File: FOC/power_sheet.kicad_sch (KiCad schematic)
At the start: 2 parts, among them U4 AP2112K-3.3

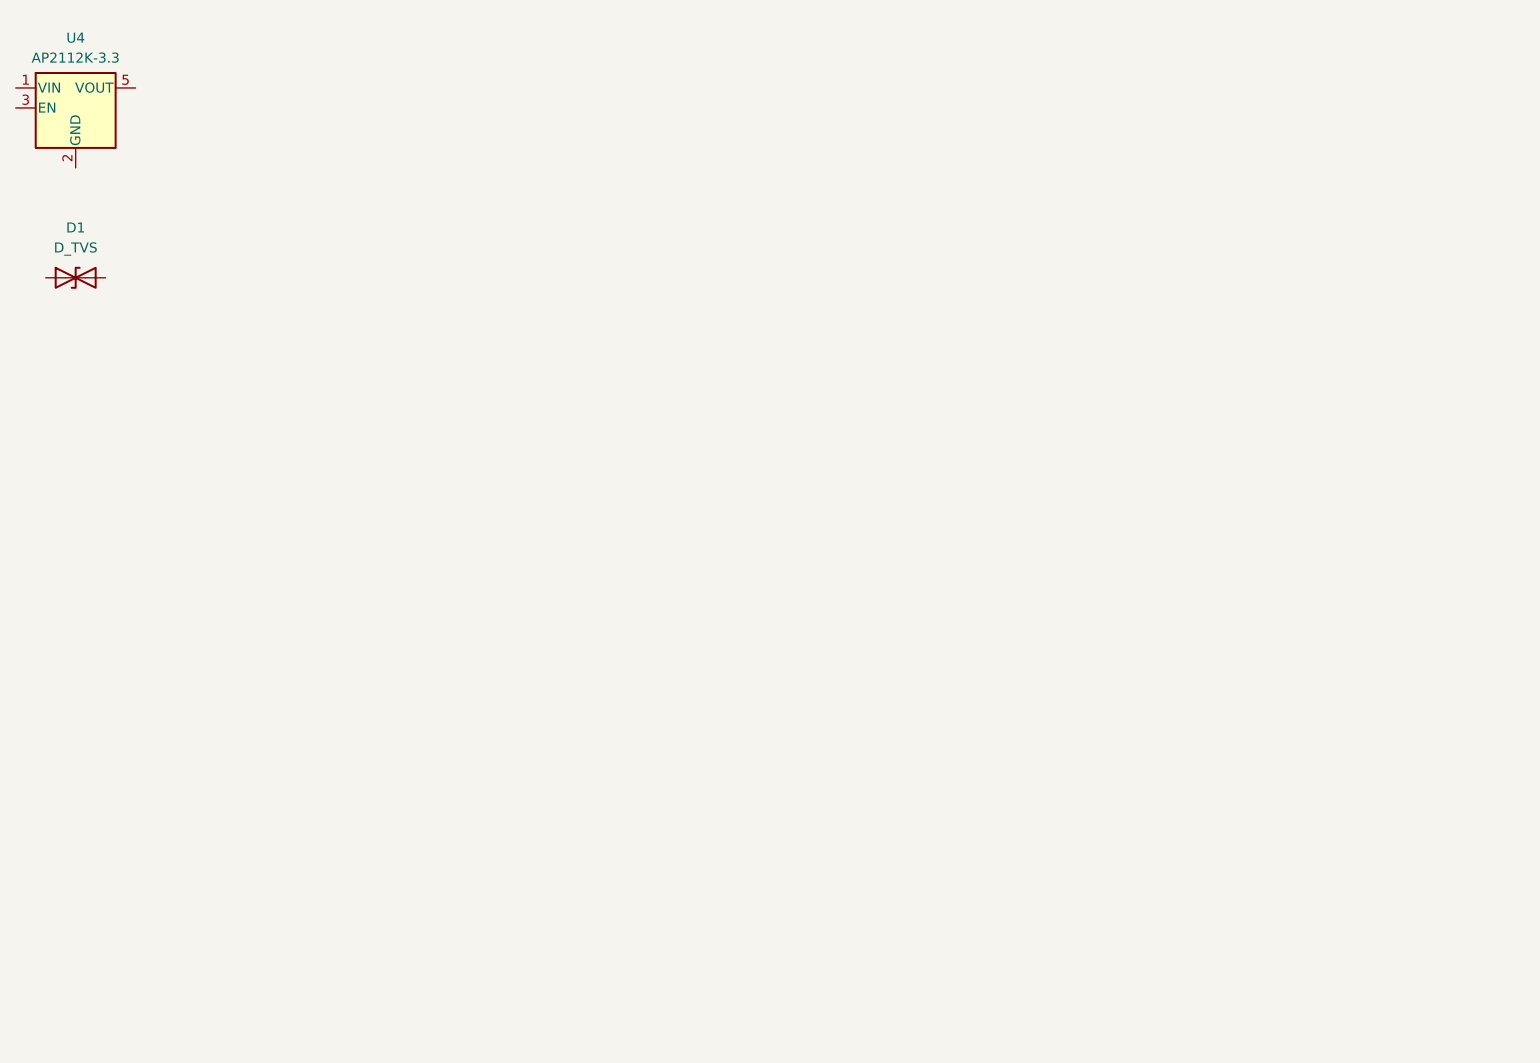
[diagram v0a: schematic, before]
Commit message: CAN + UART done;driver controller done
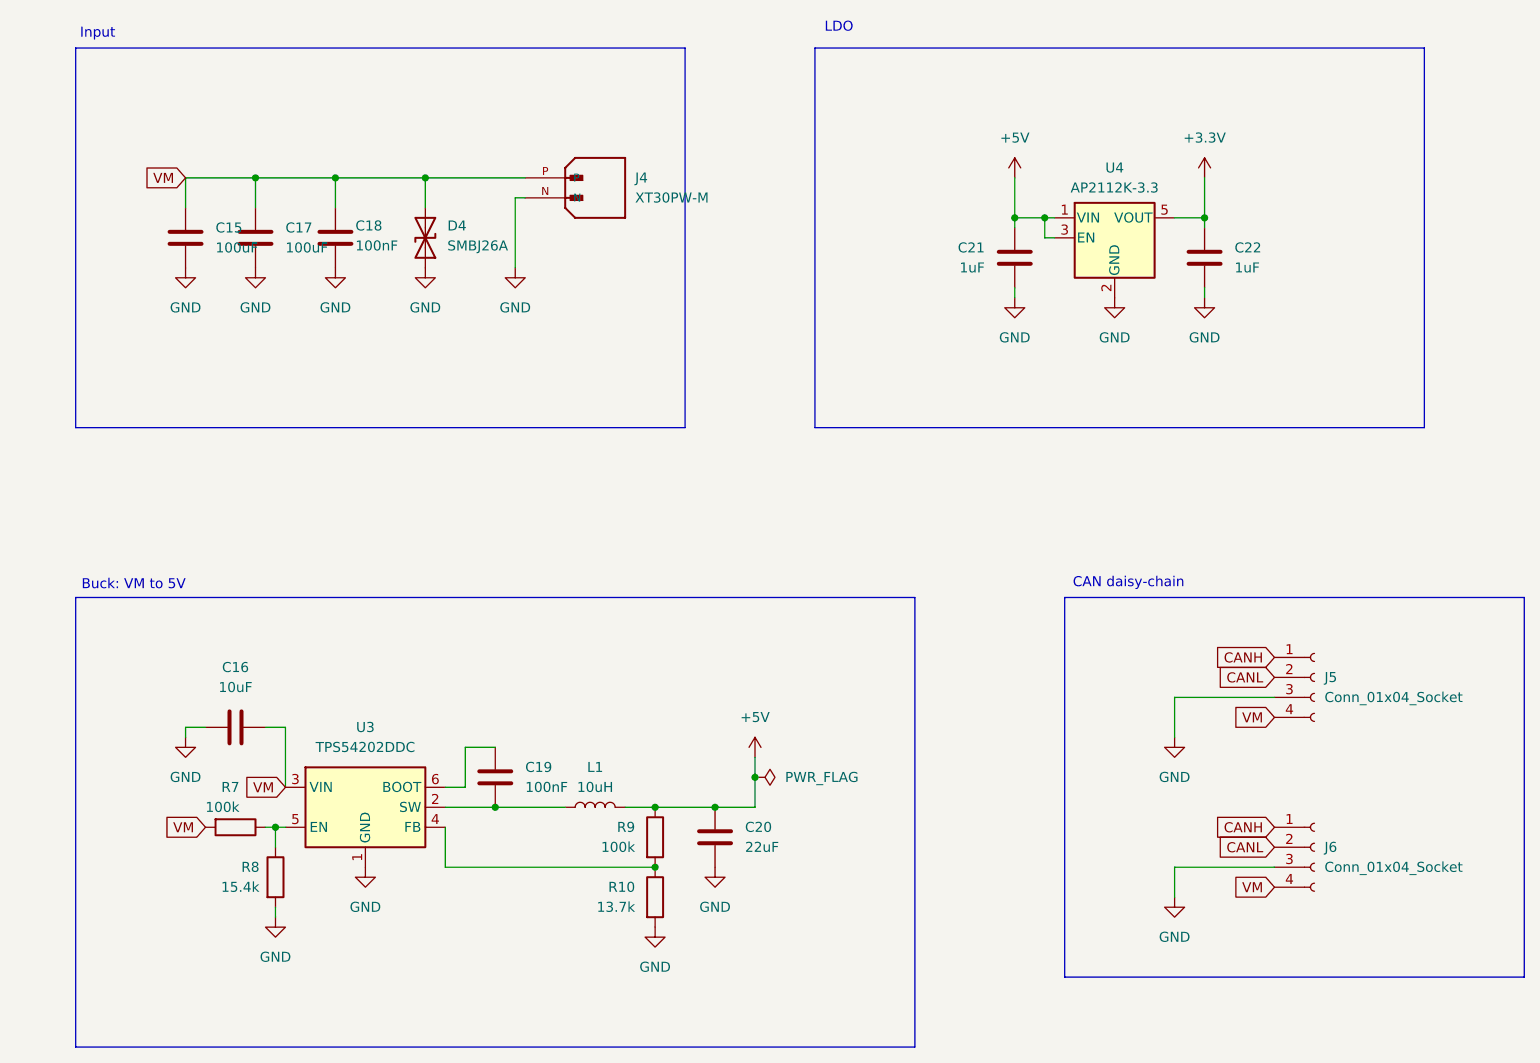
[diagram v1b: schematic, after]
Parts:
- added C15, C17: 100uF, Capacitor_SMD:CP_Elec_6.3x7.7, symbol Device:C
- added C16: 10uF, Capacitor_SMD:C_0603_1608Metric, symbol Device:C
- added C18, C19: 100nF, Capacitor_SMD:C_0603_1608Metric, symbol Device:C
- added C20: 22uF, Capacitor_SMD:C_0805_2012Metric, symbol Device:C
- added C21, C22: 1uF, Capacitor_SMD:C_0603_1608Metric, symbol Device:C
- added J4: XT30PW-M, XT30PW-M:AMASS_XT30PW-M, symbol XT30PW-M:XT30PW-M
- added J5, J6: Conn_01x04_Socket, Connector_JST:JST_GH_SM04B-GHS-TB_1x04-1MP_P1.25mm_Horizontal, symbol Connector:Conn_01x04_Socket
- added L1: 10uH, Inductor_SMD:L_Taiyo-Yuden_NR-40xx, symbol Device:L
- added R10: 13.7k, Resistor_SMD:R_0603_1608Metric, symbol Device:R
- added R7, R9: 100k, Resistor_SMD:R_0603_1608Metric, symbol Device:R
- added R8: 15.4k, Resistor_SMD:R_0603_1608Metric, symbol Device:R
- added U3: TPS54202DDC, Package_TO_SOT_SMD:SOT-23-6, symbol Regulator_Switching:TPS54202DDC
- D4: renamed from D1; value D_TVS -> SMBJ26A; footprint (none) -> Diode_SMD:D_SMB
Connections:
- net +5V: now reaches U4.1 (VIN)
- net +5V: now also U4.3 (EN), C20.1, C21.1, L1.2, R9.1
- net GND: now reaches U4.2 (GND)
- net GND: now also D4.1 (A1), C15.2, C16.1, C17.2, C18.2, C20.2, C21.2, C22.2, J4.N, J5.3 (Pin_3), J6.3 (Pin_3), R10.2, R8.2, U3.1 (GND)
- net +3.3V: now reaches U4.5 (VOUT)
- net +3.3V: now also C22.1
- net VM: now reaches D4.2 (A2)
- net VM: now also C15.1, C16.2, C17.1, C18.1, J4.P, J5.4 (Pin_4), J6.4 (Pin_4), R7.2, U3.3 (VIN)
- new net: R7.1, R8.1, U3.5 (EN)
- new net: R10.1, R9.2, U3.4 (FB)
- new net: C19.2, L1.1, U3.2 (SW)
- new net: C19.1, U3.6 (BOOT)
- new net CANH: J5.1 (Pin_1), J6.1 (Pin_1)
- new net CANL: J5.2 (Pin_2), J6.2 (Pin_2)
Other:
- note added: "Buck: VM to 5V"
- note added: "CAN daisy-chain"
- note added: "Input"
- note added: "LDO"
- moved on the sheet: D4, U4

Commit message: drc erc clean; ready to order
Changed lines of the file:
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@@
+	)
+	(junction
+		(at 97.79 52.07)
+		(diameter 0)
+		(color 0 0 0 0)
 	)
 	(junction
@@
 		)
 	)
+	(wire
+		(pts
+			(xy 97.79 52.07) (xy 105.41 52.07)
+		)
+		(stroke
+			(width 0)
+			(type default)
+		)
+	)
 	(polyline
 		(pts
@@
 	(wire
 		(pts
-			(xy 92.71 52.07) (xy 105.41 52.07)
+			(xy 92.71 52.07) (xy 97.79 52.07)
 		)
 		(stroke
@@
 					(unit 1)
 				)
+			)
+		)
+	)
+	(symbol
+		(lib_id "power:PWR_FLAG")
+		(at 97.79 52.07 0)
+		(unit 1)
+		(body_style 1)
+		(exclude_from_sim no)
+		(in_bom yes)
+		(on_board yes)
+		(in_pos_files yes)
+		(dnp no)
+		(fields_autoplaced yes)
+		(property "Reference" "#FLG011"
+			(at 97.79 50.165 0)
+			(hide yes)
+			(show_name no)
+			(do_not_autoplace no)
+			(effects
+				(font
+					(size 1.27 1.27)
+				)
+			)
+		)
+		(property "Value" "PWR_FLAG"
+			(at 97.79 46.99 0)
+			(show_name no)
+			(do_not_autoplace no)
+			(effects
+				(font
+					(size 1.27 1.27)
+				)
+			)
+		)
+		(property "Footprint" ""
+			(at 97.79 52.07 0)
+			(hide yes)
+			(show_name no)
+			(do_not_autoplace no)
+			(effects
+				(font
+					(size 1.27 1.27)
+				)
+			)
+		)
+		(property "Datasheet" ""
+			(at 97.79 52.07 0)
+			(hide yes)
+			(show_name no)
+			(do_not_autoplace no)
+			(effects
+				(font
+					(size 1.27 1.27)
+				)
+			)
+		)
+		(property "Description" "Special symbol for telling ERC where power comes from"
+			(at 97.79 52.07 0)
+			(hide yes)
+			(show_name no)
+			(do_not_autoplace no)
+			(effects
+				(font
+					(size 1.27 1.27)
+				)
+			)
+		)
+		(pin "1"
+		)
+		(instances
+			(project "FOC"
+				(path "/2261ceac-c617-4ea0-91b8-4591d1c5dbde/cae31f35-63ed-4b28-a69e-428e0122599b"
+					(reference "#FLG011")
+					(unit 1)
+				)
